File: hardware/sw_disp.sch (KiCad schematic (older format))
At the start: 20 parts, among them Q1 PMDT290UNE, SW1 GDH08S04, SW2 RST, SW3 BOOT0, SW4 USR

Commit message: things changed
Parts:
- removed D1: LTD-4708G, LTD-470:LED_LTD-4708G, symbol LTD-4708G:LTD-4708G
- removed R11, R14, R15, R5, R6, R7, R8, R9: 560, Resistor_SMD:R_0805_2012Metric, symbol Device:R_Small
- added LD1: LTD4708G, LTD-470:LED_LTD-4708G, symbol LTD-4708G:LTD4708G
- added RN1, RN2: 560, symbol Device:R_Pack04_Split
- renumbered D3 to D10, D4 to D11, D2 to D9, Q1 to Q2, R10 to R7, R12 to R8, R13 to R9
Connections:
- net labels added: Dig1, Dig2, SegA, SegB, SegC, SegD, SegDP, SegE, SegF, SegG
- net labels removed: Dig_0, Dig_1, Seg_0, Seg_1, Seg_2, Seg_3, Seg_4, Seg_5, Seg_6, Seg_7
- wire segments 58 -> 70
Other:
- moved on the sheet: Q2A, Q2B

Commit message: Changed power again
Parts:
- RN1, RN2: footprint (none) -> Resistor_SMD:R_Array_Concave_4x0603
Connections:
- net Sw_0 renamed Sw0
- net Sw_1 renamed Sw1
- net Sw_2 renamed Sw2
- net Sw_3 renamed Sw3
- net Sw_4 renamed Sw4
- net Sw_5 renamed Sw5
- net Sw_6 renamed Sw6
- net Sw_7 renamed Sw7
- net nRST renamed nReset
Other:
- moved on the sheet: SW2, SW3, SW4
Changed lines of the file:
@@
 	8100 1850 8000 1850
 Connection ~ 8100 1750
-Text HLabel 7300 1150 0    50   Output ~ 0
-Sw_0
-Text HLabel 7300 1250 0    50   Output ~ 0
-Sw_1
-Text HLabel 7300 1350 0    50   Output ~ 0
-Sw_2
-Text HLabel 7300 1450 0    50   Output ~ 0
-Sw_3
-Text HLabel 7300 1550 0    50   Output ~ 0
-Sw_4
-Text HLabel 7300 1650 0    50   Output ~ 0
-Sw_5
-Text HLabel 7300 1750 0    50   Output ~ 0
-Sw_6
-Text HLabel 7300 1850 0    50   Output ~ 0
-Sw_7
 Text HLabel 7800 2700 0    50   Input ~ 0
 Heartbeat
@@
 Wire Wire Line
 	7800 2900 8000 2900
-Text HLabel 7550 3450 0    50   Output ~ 0
-nRST
-Text HLabel 7550 3650 0    50   Output ~ 0
+Text HLabel 7850 3850 0    50   Output ~ 0
+nReset
+Text HLabel 7850 4050 0    50   Output ~ 0
 Boot0
-Text HLabel 7550 3850 0    50   Output ~ 0
+Text HLabel 7850 4250 0    50   Output ~ 0
 UserBtn
 $Comp
 L Switch:SW_Push SW2
 U 1 1 61321019
-P 7950 3450
-F 0 "SW2" H 7750 3550 50  0000 C CNN
-F 1 "RST" H 8200 3550 50  0000 C CNN
-F 2 "Button_Switch_SMD:SW_SPST_B3U-1000P" H 7950 3650 50  0001 C CNN
-F 3 "~" H 7950 3650 50  0001 C CNN
-	1    7950 3450
+P 8250 3850
+F 0 "SW2" H 8050 3950 50  0000 C CNN
+F 1 "RST" H 8500 3950 50  0000 C CNN
+F 2 "Button_Switch_SMD:SW_SPST_B3U-1000P" H 8250 4050 50  0001 C CNN
+F 3 "~" H 8250 4050 50  0001 C CNN
+	1    8250 3850
 	1    0    0    -1
 $EndComp
@@
 L Switch:SW_Push SW3
 U 1 1 61325696
-P 7950 3650
-F 0 "SW3" H 7750 3750 50  0000 C CNN
-F 1 "BOOT0" H 8200 3750 50  0000 C CNN
-F 2 "Button_Switch_SMD:SW_SPST_B3U-1000P" H 7950 3850 50  0001 C CNN
-F 3 "~" H 7950 3850 50  0001 C CNN
-	1    7950 3650
+P 8250 4050
+F 0 "SW3" H 8050 4150 50  0000 C CNN
+F 1 "BOOT0" H 8500 4150 50  0000 C CNN
+F 2 "Button_Switch_SMD:SW_SPST_B3U-1000P" H 8250 4250 50  0001 C CNN
+F 3 "~" H 8250 4250 50  0001 C CNN
+	1    8250 4050
 	1    0    0    -1
 $EndComp
@@
 L Switch:SW_Push SW4
 U 1 1 613265EF
-P 7950 3850
-F 0 "SW4" H 7750 3950 50  0000 C CNN
-F 1 "USR" H 8200 3950 50  0000 C CNN
-F 2 "Button_Switch_SMD:SW_SPST_B3U-1000P" H 7950 4050 50  0001 C CNN
-F 3 "~" H 7950 4050 50  0001 C CNN
-	1    7950 3850
-	1    0    0    -1
-$EndComp
-Wire Wire Line
-	7550 3850 7750 3850
-Wire Wire Line
-	7750 3650 7550 3650
-Wire Wire Line
-	7550 3450 7750 3450
+P 8250 4250
+F 0 "SW4" H 8050 4350 50  0000 C CNN
+F 1 "USR" H 8500 4350 50  0000 C CNN
+F 2 "Button_Switch_SMD:SW_SPST_B3U-1000P" H 8250 4450 50  0001 C CNN
+F 3 "~" H 8250 4450 50  0001 C CNN
+	1    8250 4250
+	1    0    0    -1
+$EndComp
+Wire Wire Line
+	7850 4250 8050 4250
+Wire Wire Line
+	8050 4050 7850 4050
+Wire Wire Line
+	7850 3850 8050 3850
 $Comp
 L power:GND #PWR048
 U 1 1 6132B20C
-P 8350 3950
-F 0 "#PWR048" H 8350 3700 50  0001 C CNN
-F 1 "GND" H 8355 3777 50  0000 C CNN
-F 2 "" H 8350 3950 50  0001 C CNN
-F 3 "" H 8350 3950 50  0001 C CNN
-	1    8350 3950
-	1    0    0    -1
-$EndComp
-Wire Wire Line
-	8350 3950 8350 3850
-Wire Wire Line
-	8350 3850 8150 3850
-Wire Wire Line
-	8150 3650 8350 3650
-Wire Wire Line
-	8350 3650 8350 3850
-Connection ~ 8350 3850
-Wire Wire Line
-	8150 3450 8350 3450
-Wire Wire Line
-	8350 3450 8350 3650
-Connection ~ 8350 3650
+P 8650 4350
+F 0 "#PWR048" H 8650 4100 50  0001 C CNN
+F 1 "GND" H 8655 4177 50  0000 C CNN
+F 2 "" H 8650 4350 50  0001 C CNN
+F 3 "" H 8650 4350 50  0001 C CNN
+	1    8650 4350
+	1    0    0    -1
+$EndComp
+Wire Wire Line
+	8650 4350 8650 4250
+Wire Wire Line
+	8650 4250 8450 4250
+Wire Wire Line
+	8450 4050 8650 4050
+Wire Wire Line
+	8650 4050 8650 4250
+Connection ~ 8650 4250
+Wire Wire Line
+	8450 3850 8650 3850
+Wire Wire Line
+	8650 3850 8650 4050
+Connection ~ 8650 4050
 $Comp
 L Device:LED D9
@@
 F 0 "RN1" V 1800 3800 50  0000 L CNN
 F 1 "560" V 1850 3650 50  0000 C CNN
-F 2 "" V 1770 3650 50  0001 C CNN
+F 2 "Resistor_SMD:R_Array_Concave_4x0603" V 1770 3650 50  0001 C CNN
 F 3 "~" H 1850 3650 50  0001 C CNN
 	3    1850 3650
@@
 F 0 "RN2" V 2300 3800 50  0000 L CNN
 F 1 "560" V 2350 3650 50  0000 C CNN
-F 2 "" V 2270 3650 50  0001 C CNN
+F 2 "Resistor_SMD:R_Array_Concave_4x0603" V 2270 3650 50  0001 C CNN
 F 3 "~" H 2350 3650 50  0001 C CNN
 	4    2350 3650
@@
 F 0 "RN2" V 2000 3800 50  0000 L CNN
 F 1 "560" V 2050 3650 50  0000 C CNN
-F 2 "" V 1970 3650 50  0001 C CNN
+F 2 "Resistor_SMD:R_Array_Concave_4x0603" V 1970 3650 50  0001 C CNN
 F 3 "~" H 2050 3650 50  0001 C CNN
 	1    2050 3650
@@
 F 0 "RN1" V 1900 3800 50  0000 L CNN
 F 1 "560" V 1950 3650 50  0000 C CNN
-F 2 "" V 1870 3650 50  0001 C CNN
+F 2 "Resistor_SMD:R_Array_Concave_4x0603" V 1870 3650 50  0001 C CNN
 F 3 "~" H 1950 3650 50  0001 C CNN
 	4    1950 3650
@@
 F 0 "RN2" V 2100 3800 50  0000 L CNN
 F 1 "560" V 2150 3650 50  0000 C CNN
-F 2 "" V 2070 3650 50  0001 C CNN
+F 2 "Resistor_SMD:R_Array_Concave_4x0603" V 2070 3650 50  0001 C CNN
 F 3 "~" H 2150 3650 50  0001 C CNN
 	2    2150 3650
@@
 F 0 "RN2" V 2200 3800 50  0000 L CNN
 F 1 "560" V 2250 3650 50  0000 C CNN
-F 2 "" V 2170 3650 50  0001 C CNN
+F 2 "Resistor_SMD:R_Array_Concave_4x0603" V 2170 3650 50  0001 C CNN
 F 3 "~" H 2250 3650 50  0001 C CNN
 	3    2250 3650
@@
 F 0 "RN1" V 1700 3800 50  0000 L CNN
 F 1 "560" V 1750 3650 50  0000 C CNN
-F 2 "" V 1670 3650 50  0001 C CNN
+F 2 "Resistor_SMD:R_Array_Concave_4x0603" V 1670 3650 50  0001 C CNN
 F 3 "~" H 1750 3650 50  0001 C CNN
 	2    1750 3650
@@
 F 0 "RN1" V 1600 3800 50  0000 L CNN
 F 1 "560" V 1650 3650 50  0000 C CNN
-F 2 "" V 1570 3650 50  0001 C CNN
+F 2 "Resistor_SMD:R_Array_Concave_4x0603" V 1570 3650 50  0001 C CNN
 F 3 "~" H 1650 3650 50  0001 C CNN
 	1    1650 3650
 	1    0    0    -1
 $EndComp
+Text HLabel 7300 1150 0    50   Output ~ 0
+Sw0
+Text HLabel 7300 1250 0    50   Output ~ 0
+Sw1
+Text HLabel 7300 1350 0    50   Output ~ 0
+Sw2
+Text HLabel 7300 1450 0    50   Output ~ 0
+Sw3
+Text HLabel 7300 1550 0    50   Output ~ 0
+Sw4
+Text HLabel 7300 1650 0    50   Output ~ 0
+Sw5
+Text HLabel 7300 1750 0    50   Output ~ 0
+Sw6
+Text HLabel 7300 1850 0    50   Output ~ 0
+Sw7
 $EndSCHEMATC

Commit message: Started routing
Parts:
- removed SW2: RST, Button_Switch_SMD:SW_SPST_B3U-1000P, symbol Switch:SW_Push
- removed SW3: BOOT0, Button_Switch_SMD:SW_SPST_B3U-1000P, symbol Switch:SW_Push
- removed SW4: USR, Button_Switch_SMD:SW_SPST_B3U-1000P, symbol Switch:SW_Push
- added R18, R19: 10k, Resistor_SMD:R_0805_2012Metric, symbol Device:R_Small
- added SW2: Boot0, RKB2SJ:RKB2SJ, symbol Switch:SW_Push_45deg
- added SW3: User, RKB2SJ:RKB2SJ, symbol Switch:SW_Push_45deg
- added SW4: nReset, RKB2SJ:RKB2SJ, symbol Switch:SW_Push_45deg
- SW1: value GDH08S04 -> 218-8LPS; footprint GDH08S04:SOIC127P813X256-16N -> Button_Switch_SMD:SW_DIP_SPSTx08_Slide_KingTek_DSHP08TS_W7.62mm_P1.27mm
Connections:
- net +3V3: now also R19.2, SW2.2, SW3.2
- net Boot0: now also R18.1, SW2.1
- net GND: now also R18.2, SW4.2
- net UserBtn: now also SW3.1
- net nReset: now also R19.1, SW4.1
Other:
- note added: "RKB2SJx250SMTR"
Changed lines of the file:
@@
 P 7700 1550
 F 0 "SW1" H 7700 2217 50  0000 C CNN
-F 1 "GDH08S04" H 7700 2126 50  0000 C CNN
-F 2 "GDH08S04:SOIC127P813X256-16N" H 7700 1550 50  0001 C CNN
-F 3 "~" H 7700 1550 50  0001 C CNN
+F 1 "218-8LPS" H 7700 2126 50  0000 C CNN
+F 2 "Button_Switch_SMD:SW_DIP_SPSTx08_Slide_KingTek_DSHP08TS_W7.62mm_P1.27mm" H 7700 1550 50  0001 C CNN
+F 3 "https://www.ctscorp.com/wp-content/uploads/218.pdf" H 7700 1550 50  0001 C CNN
 	1    7700 1550
 	1    0    0    -1
@@
 Wire Wire Line
 	7800 2900 8000 2900
-Text HLabel 7850 3850 0    50   Output ~ 0
+Text HLabel 6000 4700 3    50   Output ~ 0
 nReset
-Text HLabel 7850 4050 0    50   Output ~ 0
+Text HLabel 5000 4700 3    50   Output ~ 0
 Boot0
-Text HLabel 7850 4250 0    50   Output ~ 0
+Text HLabel 5500 4700 3    50   Output ~ 0
 UserBtn
-$Comp
-L Switch:SW_Push SW2
-U 1 1 61321019
-P 8250 3850
-F 0 "SW2" H 8050 3950 50  0000 C CNN
-F 1 "RST" H 8500 3950 50  0000 C CNN
-F 2 "Button_Switch_SMD:SW_SPST_B3U-1000P" H 8250 4050 50  0001 C CNN
-F 3 "~" H 8250 4050 50  0001 C CNN
-	1    8250 3850
-	1    0    0    -1
-$EndComp
-$Comp
-L Switch:SW_Push SW3
-U 1 1 61325696
-P 8250 4050
-F 0 "SW3" H 8050 4150 50  0000 C CNN
-F 1 "BOOT0" H 8500 4150 50  0000 C CNN
-F 2 "Button_Switch_SMD:SW_SPST_B3U-1000P" H 8250 4250 50  0001 C CNN
-F 3 "~" H 8250 4250 50  0001 C CNN
-	1    8250 4050
-	1    0    0    -1
-$EndComp
-$Comp
-L Switch:SW_Push SW4
-U 1 1 613265EF
-P 8250 4250
-F 0 "SW4" H 8050 4350 50  0000 C CNN
-F 1 "USR" H 8500 4350 50  0000 C CNN
-F 2 "Button_Switch_SMD:SW_SPST_B3U-1000P" H 8250 4450 50  0001 C CNN
-F 3 "~" H 8250 4450 50  0001 C CNN
-	1    8250 4250
-	1    0    0    -1
-$EndComp
-Wire Wire Line
-	7850 4250 8050 4250
-Wire Wire Line
-	8050 4050 7850 4050
-Wire Wire Line
-	7850 3850 8050 3850
-$Comp
-L power:GND #PWR048
-U 1 1 6132B20C
-P 8650 4350
-F 0 "#PWR048" H 8650 4100 50  0001 C CNN
-F 1 "GND" H 8655 4177 50  0000 C CNN
-F 2 "" H 8650 4350 50  0001 C CNN
-F 3 "" H 8650 4350 50  0001 C CNN
-	1    8650 4350
-	1    0    0    -1
-$EndComp
-Wire Wire Line
-	8650 4350 8650 4250
-Wire Wire Line
-	8650 4250 8450 4250
-Wire Wire Line
-	8450 4050 8650 4050
-Wire Wire Line
-	8650 4050 8650 4250
-Connection ~ 8650 4250
-Wire Wire Line
-	8450 3850 8650 3850
-Wire Wire Line
-	8650 3850 8650 4050
-Connection ~ 8650 4050
 $Comp
 L Device:LED D9
@@
 Text HLabel 7300 1850 0    50   Output ~ 0
 Sw7
+$Comp
+L Device:R_Small R18
+U 1 1 6134B08F
+P 5100 4800
+F 0 "R18" H 5159 4846 50  0000 L CNN
+F 1 "10k" H 5159 4755 50  0000 L CNN
+F 2 "Resistor_SMD:R_0805_2012Metric" H 5100 4800 50  0001 C CNN
+F 3 "~" H 5100 4800 50  0001 C CNN
+	1    5100 4800
+	1    0    0    -1
+$EndComp
+$Comp
+L Switch:SW_Push_45deg SW2
+U 1 1 6134E9D2
+P 5100 4400
+F 0 "SW2" V 5150 4300 50  0000 R CNN
+F 1 "Boot0" V 5050 4350 50  0000 R CNN
+F 2 "RKB2SJ:RKB2SJ" H 5100 4400 50  0001 C CNN
+F 3 "https://hu.mouser.com/datasheet/2/60/ck_rk_datasheet-2295758.pdf" H 5100 4400 50  0001 C CNN
+	1    5100 4400
+	0    -1   -1   0
+$EndComp
+$Comp
+L Device:R_Small R19
+U 1 1 613506CF
+P 6100 4800
+F 0 "R19" H 6159 4846 50  0000 L CNN
+F 1 "10k" H 6159 4755 50  0000 L CNN
+F 2 "Resistor_SMD:R_0805_2012Metric" H 6100 4800 50  0001 C CNN
+F 3 "~" H 6100 4800 50  0001 C CNN
+	1    6100 4800
+	1    0    0    -1
+$EndComp
+Wire Wire Line
+	6000 4500 6000 4600
+Wire Wire Line
+	5000 4500 5000 4600
+Wire Wire Line
+	5000 4600 5100 4600
+Wire Wire Line
+	5100 4600 5100 4700
+Connection ~ 5000 4600
+Wire Wire Line
+	5000 4600 5000 4700
+Wire Wire Line
+	5500 4500 5500 4700
+Wire Wire Line
+	6000 4600 6100 4600
+Wire Wire Line
+	6100 4600 6100 4700
+Wire Wire Line
+	6000 4700 6000 4600
+Connection ~ 6000 4600
+$Comp
+L power:+3.3V #PWR0104
+U 1 1 6136858B
+P 5200 4200
+F 0 "#PWR0104" H 5200 4050 50  0001 C CNN
+F 1 "+3.3V" H 5200 4350 50  0000 C CNN
+F 2 "" H 5200 4200 50  0001 C CNN
+F 3 "" H 5200 4200 50  0001 C CNN
+	1    5200 4200
+	1    0    0    -1
+$EndComp
+$Comp
+L power:+3.3V #PWR0105
+U 1 1 61368CC2
+P 5700 4200
+F 0 "#PWR0105" H 5700 4050 50  0001 C CNN
+F 1 "+3.3V" H 5700 4350 50  0000 C CNN
+F 2 "" H 5700 4200 50  0001 C CNN
+F 3 "" H 5700 4200 50  0001 C CNN
+	1    5700 4200
+	1    0    0    -1
+$EndComp
+$Comp
+L power:GND #PWR0106
+U 1 1 613698D1
+P 6200 4200
+F 0 "#PWR0106" H 6200 3950 50  0001 C CNN
+F 1 "GND" H 6200 4050 50  0000 C CNN
+F 2 "" H 6200 4200 50  0001 C CNN
+F 3 "" H 6200 4200 50  0001 C CNN
+	1    6200 4200
+	-1   0    0    1
+$EndComp
+Wire Wire Line
+	6200 4200 6200 4300
+Wire Wire Line
+	5700 4200 5700 4300
+Wire Wire Line
+	5200 4200 5200 4300
+$Comp
+L power:GND #PWR0107
+U 1 1 61370459
+P 5100 5000
+F 0 "#PWR0107" H 5100 4750 50  0001 C CNN
+F 1 "GND" H 5100 4850 50  0000 C CNN
+F 2 "" H 5100 5000 50  0001 C CNN
+F 3 "" H 5100 5000 50  0001 C CNN
+	1    5100 5000
+	1    0    0    -1
+$EndComp
+$Comp
+L power:+3.3V #PWR0108
+U 1 1 61370BAA
+P 6100 5000
+F 0 "#PWR0108" H 6100 4850 50  0001 C CNN
+F 1 "+3.3V" H 6100 5150 50  0000 C CNN
+F 2 "" H 6100 5000 50  0001 C CNN
+F 3 "" H 6100 5000 50  0001 C CNN
+	1    6100 5000
+	-1   0    0    1
+$EndComp
+Wire Wire Line
+	6100 4900 6100 5000
+Wire Wire Line
+	5100 4900 5100 5000
+$Comp
+L Switch:SW_Push_45deg SW3
+U 1 1 613767DB
+P 5600 4400
+F 0 "SW3" V 5650 4300 50  0000 R CNN
+F 1 "User" V 5550 4350 50  0000 R CNN
+F 2 "RKB2SJ:RKB2SJ" H 5600 4400 50  0001 C CNN
+F 3 "https://hu.mouser.com/datasheet/2/60/ck_rk_datasheet-2295758.pdf" H 5600 4400 50  0001 C CNN
+	1    5600 4400
+	0    -1   -1   0
+$EndComp
+$Comp
+L Switch:SW_Push_45deg SW4
+U 1 1 61376EA7
+P 6100 4400
+F 0 "SW4" V 6150 4300 50  0000 R CNN
+F 1 "nReset" V 6050 4350 50  0000 R CNN
+F 2 "RKB2SJ:RKB2SJ" H 6100 4400 50  0001 C CNN
+F 3 "https://hu.mouser.com/datasheet/2/60/ck_rk_datasheet-2295758.pdf" H 6100 4400 50  0001 C CNN
+	1    6100 4400
+	0    -1   -1   0
+$EndComp
+Text Notes 6400 4150 0    50   ~ 0
+RKB2SJx250SMTR
 $EndSCHEMATC

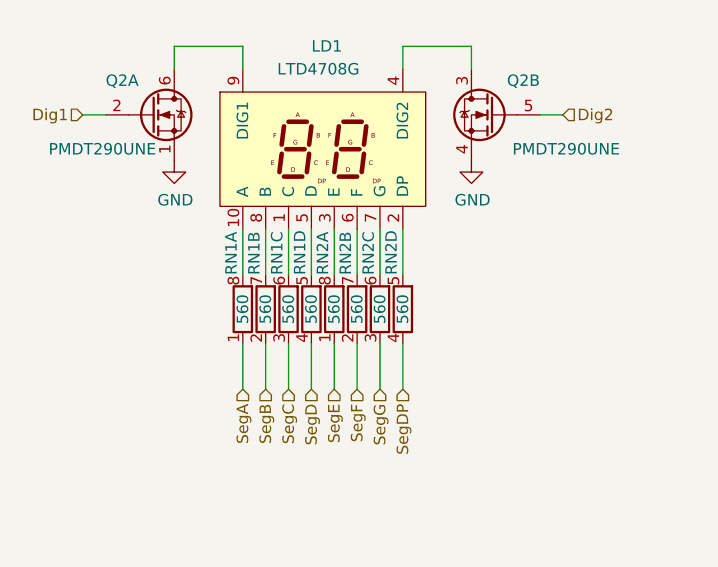
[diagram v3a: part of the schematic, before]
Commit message: Power routing
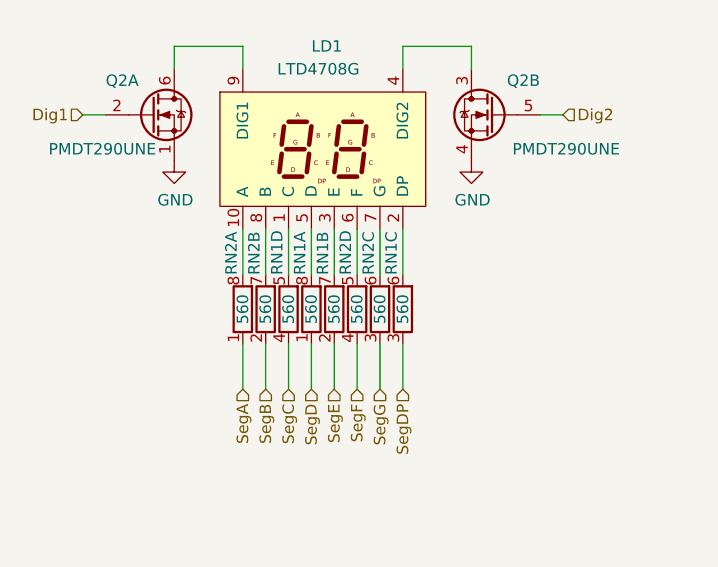
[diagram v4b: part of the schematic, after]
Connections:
- net SegA: now also RN2.1 (R1.1); no longer RN1.1 (R1.1)
- net SegB: now also RN2.2 (R2.1); no longer RN1.2 (R2.1)
- net SegC: now also RN1.4 (R4.1); no longer RN1.3 (R3.1)
- net SegD: now also RN1.1 (R1.1); no longer RN1.4 (R4.1)
- net SegDP: now also RN1.3 (R3.1); no longer RN2.4 (R4.1)
- net SegE: now also RN1.2 (R2.1); no longer RN2.1 (R1.1)
- net SegF: now also RN2.4 (R4.1); no longer RN2.2 (R2.1)
- net at LD1.1 (C): now also RN1.5 (R4.2); no longer RN1.6 (R3.2)
- net at LD1.10 (A): now also RN2.8 (R1.2); no longer RN1.8 (R1.2)
- net at LD1.2 (DP): now also RN1.6 (R3.2); no longer RN2.5 (R4.2)
- net at LD1.3 (E): now also RN1.7 (R2.2); no longer RN2.8 (R1.2)
- net at LD1.5 (D): now also RN1.8 (R1.2); no longer RN1.5 (R4.2)
- net at LD1.6 (F): now also RN2.5 (R4.2); no longer RN2.7 (R2.2)
- net at LD1.8 (B): now also RN2.7 (R2.2); no longer RN1.7 (R2.2)
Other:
- moved on the sheet: RN1A, RN1B, RN1C, RN1D, RN2A, RN2B, RN2D
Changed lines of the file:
@@
 L Device:R_Pack04_Split RN1
 U 3 1 612DF692
+P 2350 3650
+F 0 "RN1" V 2300 3800 50  0000 L CNN
+F 1 "560" V 2350 3650 50  0000 C CNN
+F 2 "Resistor_SMD:R_Array_Concave_4x0603" V 2270 3650 50  0001 C CNN
+F 3 "~" H 2350 3650 50  0001 C CNN
+	3    2350 3650
+	1    0    0    -1
+$EndComp
+$Comp
+L Device:R_Pack04_Split RN2
+U 4 1 612E0F78
+P 2150 3650
+F 0 "RN2" V 2100 3800 50  0000 L CNN
+F 1 "560" V 2150 3650 50  0000 C CNN
+F 2 "Resistor_SMD:R_Array_Concave_4x0603" V 2070 3650 50  0001 C CNN
+F 3 "~" H 2150 3650 50  0001 C CNN
+	4    2150 3650
+	1    0    0    -1
+$EndComp
+$Comp
+L Device:R_Pack04_Split RN2
+U 1 1 612E22C4
+P 1650 3650
+F 0 "RN2" V 1600 3800 50  0000 L CNN
+F 1 "560" V 1650 3650 50  0000 C CNN
+F 2 "Resistor_SMD:R_Array_Concave_4x0603" V 1570 3650 50  0001 C CNN
+F 3 "~" H 1650 3650 50  0001 C CNN
+	1    1650 3650
+	1    0    0    -1
+$EndComp
+$Comp
+L Device:R_Pack04_Split RN1
+U 4 1 612E26A3
 P 1850 3650
 F 0 "RN1" V 1800 3800 50  0000 L CNN
@@
 F 2 "Resistor_SMD:R_Array_Concave_4x0603" V 1770 3650 50  0001 C CNN
 F 3 "~" H 1850 3650 50  0001 C CNN
-	3    1850 3650
-	1    0    0    -1
-$EndComp
-$Comp
-L Device:R_Pack04_Split RN2
-U 4 1 612E0F78
-P 2350 3650
-F 0 "RN2" V 2300 3800 50  0000 L CNN
-F 1 "560" V 2350 3650 50  0000 C CNN
-F 2 "Resistor_SMD:R_Array_Concave_4x0603" V 2270 3650 50  0001 C CNN
-F 3 "~" H 2350 3650 50  0001 C CNN
-	4    2350 3650
-	1    0    0    -1
-$EndComp
-$Comp
-L Device:R_Pack04_Split RN2
-U 1 1 612E22C4
-P 2050 3650
-F 0 "RN2" V 2000 3800 50  0000 L CNN
-F 1 "560" V 2050 3650 50  0000 C CNN
-F 2 "Resistor_SMD:R_Array_Concave_4x0603" V 1970 3650 50  0001 C CNN
-F 3 "~" H 2050 3650 50  0001 C CNN
-	1    2050 3650
-	1    0    0    -1
-$EndComp
-$Comp
-L Device:R_Pack04_Split RN1
-U 4 1 612E26A3
-P 1950 3650
-F 0 "RN1" V 1900 3800 50  0000 L CNN
-F 1 "560" V 1950 3650 50  0000 C CNN
-F 2 "Resistor_SMD:R_Array_Concave_4x0603" V 1870 3650 50  0001 C CNN
-F 3 "~" H 1950 3650 50  0001 C CNN
-	4    1950 3650
+	4    1850 3650
 	1    0    0    -1
 $EndComp
@@
 L Device:R_Pack04_Split RN2
 U 2 1 612E8557
-P 2150 3650
-F 0 "RN2" V 2100 3800 50  0000 L CNN
-F 1 "560" V 2150 3650 50  0000 C CNN
-F 2 "Resistor_SMD:R_Array_Concave_4x0603" V 2070 3650 50  0001 C CNN
-F 3 "~" H 2150 3650 50  0001 C CNN
-	2    2150 3650
+P 1750 3650
+F 0 "RN2" V 1700 3800 50  0000 L CNN
+F 1 "560" V 1750 3650 50  0000 C CNN
+F 2 "Resistor_SMD:R_Array_Concave_4x0603" V 1670 3650 50  0001 C CNN
+F 3 "~" H 1750 3650 50  0001 C CNN
+	2    1750 3650
 	1    0    0    -1
 $EndComp
@@
 L Device:R_Pack04_Split RN1
 U 2 1 612E8563
-P 1750 3650
-F 0 "RN1" V 1700 3800 50  0000 L CNN
-F 1 "560" V 1750 3650 50  0000 C CNN
-F 2 "Resistor_SMD:R_Array_Concave_4x0603" V 1670 3650 50  0001 C CNN
-F 3 "~" H 1750 3650 50  0001 C CNN
-	2    1750 3650
+P 2050 3650
+F 0 "RN1" V 2000 3800 50  0000 L CNN
+F 1 "560" V 2050 3650 50  0000 C CNN
+F 2 "Resistor_SMD:R_Array_Concave_4x0603" V 1970 3650 50  0001 C CNN
+F 3 "~" H 2050 3650 50  0001 C CNN
+	2    2050 3650
 	1    0    0    -1
 $EndComp
@@
 L Device:R_Pack04_Split RN1
 U 1 1 612E8569
-P 1650 3650
-F 0 "RN1" V 1600 3800 50  0000 L CNN
-F 1 "560" V 1650 3650 50  0000 C CNN
-F 2 "Resistor_SMD:R_Array_Concave_4x0603" V 1570 3650 50  0001 C CNN
-F 3 "~" H 1650 3650 50  0001 C CNN
-	1    1650 3650
+P 1950 3650
+F 0 "RN1" V 1900 3800 50  0000 L CNN
+F 1 "560" V 1950 3650 50  0000 C CNN
+F 2 "Resistor_SMD:R_Array_Concave_4x0603" V 1870 3650 50  0001 C CNN
+F 3 "~" H 1950 3650 50  0001 C CNN
+	1    1950 3650
 	1    0    0    -1
 $EndComp
